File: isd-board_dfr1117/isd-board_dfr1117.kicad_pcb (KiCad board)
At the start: 2 copper layers, 90 x 50 mm, 46 parts, among them J1 BATT, J2 Conn_01x08, J3 Conn_01x02_Pin, J4 Conn_01x08, J5 Conn_01x04, J6 Conn_01x04, J7 Conn_01x05, J8 USB_C_Receptacle_PowerOnly_6P, Q1 Q_Dual_NMOS_S1G1D2S2G2D1, Q3 AO3401A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

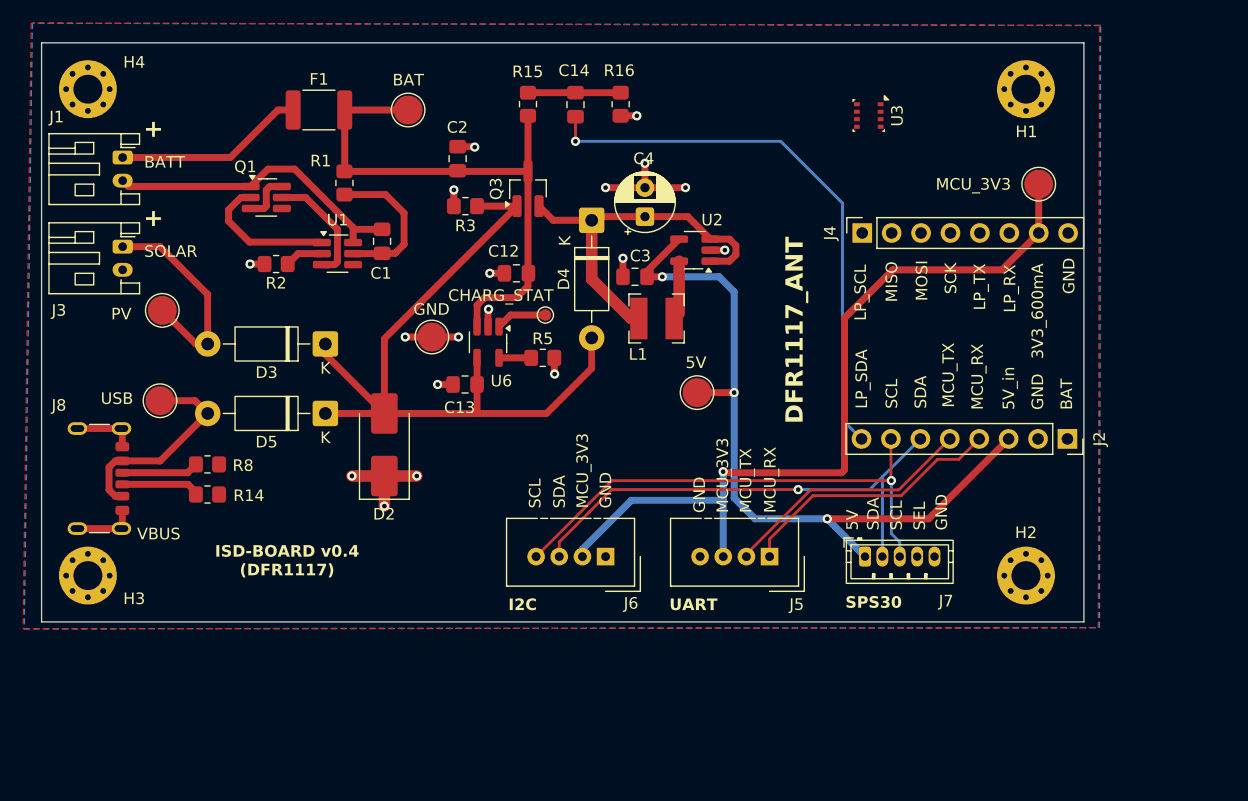
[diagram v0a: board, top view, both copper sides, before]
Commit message: update: battery protection circuit (compact placement)
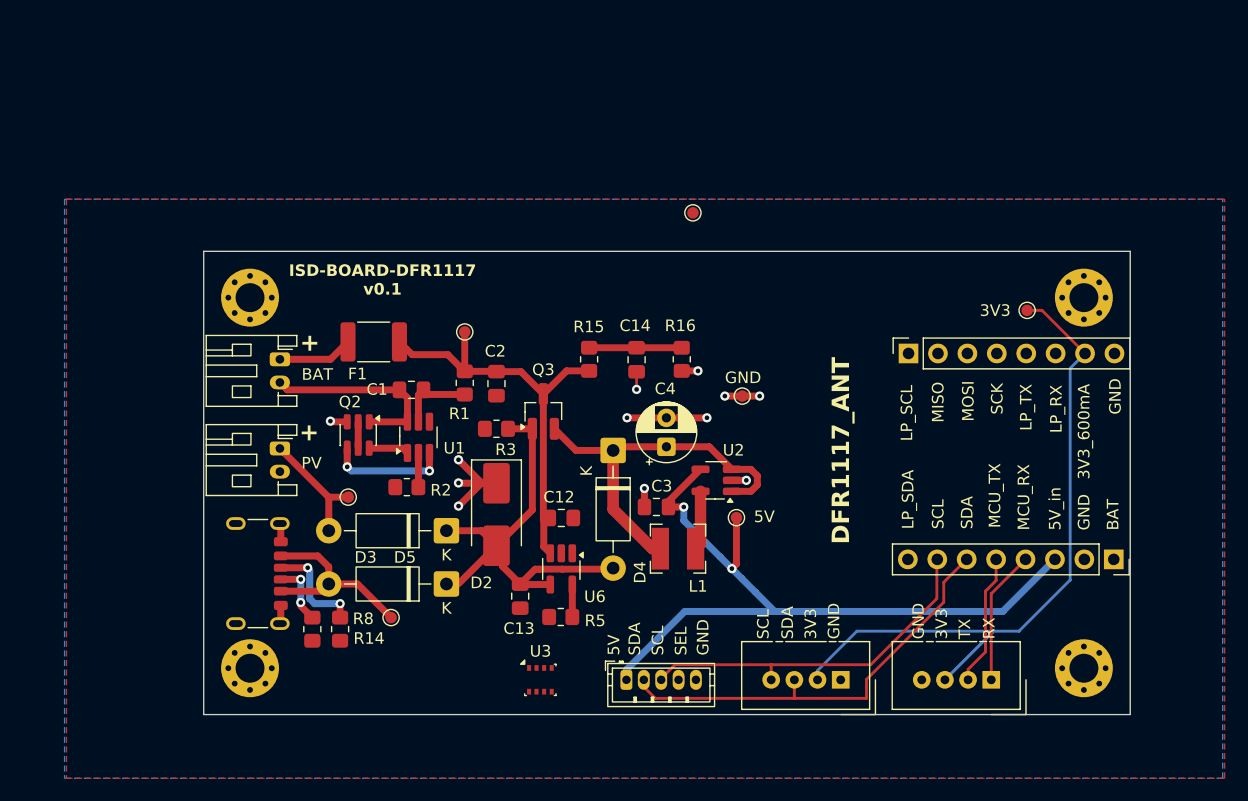
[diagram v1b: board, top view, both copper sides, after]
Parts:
- removed Q1: Q_Dual_NMOS_S1G1D2S2G2D1, Package_TO_SOT_SMD:SOT-23-6_Handsoldering
- added Q2: DMG9926UDM, Package_TO_SOT_SMD:SOT-23-6, F.Cu at (118.3, 75.9)
- TP2, TP3, TP4, TP5, TP6, TP7: footprint TestPoint:TestPoint_Pad_D2.5mm -> TestPoint:TestPoint_Pad_D1.0mm
- moved U3 56.4 mm to (134.1, 97.0), turned to 0 degrees
- moved TP2 27.4 mm to (121.2, 91.6)
- moved TP4 27.3 mm to (151.5, 72.5)
- moved J7 23.2 mm to (141.5, 97.0)
- moved J6 22.9 mm to (160.0, 97.0)
- moved H4 22.8 mm to (109.0, 64.0)
- moved TP3 22.8 mm to (117.5, 81.2)
- moved R15 22.6 mm to (138.3, 69.3)
- moved R16 22.6 mm to (146.3, 69.3)
- moved C14 22.6 mm to (142.4, 69.4)
- moved R5 22.4 mm to (135.8, 91.6), turned to 180 degrees
- moved R2 22.3 mm to (122.5, 80.4)
- moved J1 22.1 mm to (111.6, 69.3)
- moved J3 22.1 mm to (111.6, 77.0)
- moved J5 21.9 mm to (173.0, 97.0)
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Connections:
- U3 pad 2: +3V3 -> MCU_3V3
- U3 pad 6: +3V3 -> MCU_3V3
- U3 pad 8: +3V3 -> MCU_3V3
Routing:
- net /LP_SDA: track 48.5 -> 1.56 mm
- net /V_PWRMAN: track 66.6 -> 41.1 mm
- net GND: track 46.9 -> 30.6 mm, vias 18 -> 11
- net /SCL: track 43.9 -> 31.5 mm, vias 1 -> 0
- net +BATT: track 48.3 -> 36.5 mm
- net /MCU_RX: track 23.2 -> 11.6 mm
- net MCU_3V3: track 69.6 -> 58.4 mm, vias 1 -> 0
- net /MCU_TX: track 21.9 -> 11.4 mm
- net Net-(J1-Pin_1): track 16.4 -> 6.50 mm
- net Net-(J1-Pin_2): track 26.7 -> 16.9 mm
- net Net-(Q2-G1): track 12.1 -> 3.47 mm
- net /V_SOLAR: track 18.5 -> 10.5 mm
- net Net-(U1-VCC): track 13.2 -> 6.66 mm
- net /SDA: track 43.0 -> 37.4 mm, vias 1 -> 0
- net Net-(U6-STAT): track 4.41 -> 0.00 mm
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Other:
- board size 90 x 50 mm -> 80 x 40 mm
- board text added: "3V3"
- board text added: "ISD-BOARD-DFR1117 v0.1"
- board text added: "RX"
- board text added: "TX"
- board text removed: "BATT"
- board text removed: "CHARG_STAT"
- board text removed: "I2C"
- board text removed: "ISD-BOARD v0.4 (DFR1117)"
- board text removed: "MCU_3V3"
- board text removed: "SOLAR"
- board text removed: "SPS30"
- board text removed: "UART"
- board text removed: "USB"
- board text removed: "VBUS"
